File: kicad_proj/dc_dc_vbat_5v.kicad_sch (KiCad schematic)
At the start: 14 parts, among them U4 TPS563200

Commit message: checked root, dc dc and rpi sheets
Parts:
- renumbered R19 to R8, TP6 to TP8, TP7 to TP9
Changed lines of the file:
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@@
 		(dnp no)
 		(fields_autoplaced yes)
-		(property "Reference" "#PWR22"
+		(property "Reference" "#PWR21"
 			(at 172.72 99.06 0)
 			(effects
@@
 			(project "rpi_power_warden_hat"
 				(path "/8692c5de-a943-41e8-8e29-f6c5e99cda34/5bbc6f2d-46db-4213-8835-1ada71ba8330"
-					(reference "#PWR22")
-					(unit 1)
-				)
-				(path "/8692c5de-a943-41e8-8e29-f6c5e99cda34/cc58a92a-1392-4aa4-91cc-7a70ded8904f"
-					(reference "#PWR29")
+					(reference "#PWR21")
+					(unit 1)
+				)
+				(path "/8692c5de-a943-41e8-8e29-f6c5e99cda34/cc58a92a-1392-4aa4-91cc-7a70ded8904f"
+					(reference "#PWR28")
 					(unit 1)
 				)
@@
 		(dnp no)
 		(fields_autoplaced yes)
-		(property "Reference" "#PWR21"
+		(property "Reference" "#PWR20"
 			(at 128.27 101.6 0)
 			(effects
@@
 			(project "rpi_power_warden_hat"
 				(path "/8692c5de-a943-41e8-8e29-f6c5e99cda34/5bbc6f2d-46db-4213-8835-1ada71ba8330"
-					(reference "#PWR21")
-					(unit 1)
-				)
-				(path "/8692c5de-a943-41e8-8e29-f6c5e99cda34/cc58a92a-1392-4aa4-91cc-7a70ded8904f"
-					(reference "#PWR28")
+					(reference "#PWR20")
+					(unit 1)
+				)
+				(path "/8692c5de-a943-41e8-8e29-f6c5e99cda34/cc58a92a-1392-4aa4-91cc-7a70ded8904f"
+					(reference "#PWR27")
 					(unit 1)
 				)
@@
 		(dnp no)
 		(fields_autoplaced yes)
-		(property "Reference" "TP7"
-			(at 181.61 77.9779 0)
+		(property "Reference" "TP9"
+			(at 181.61 79.2479 0)
 			(effects
 				(font
@@
 				)
 				(justify left)
+				(hide yes)
 			)
 		)
@@
 			(project "rpi_power_warden_hat"
 				(path "/8692c5de-a943-41e8-8e29-f6c5e99cda34/5bbc6f2d-46db-4213-8835-1ada71ba8330"
-					(reference "TP7")
-					(unit 1)
-				)
-				(path "/8692c5de-a943-41e8-8e29-f6c5e99cda34/cc58a92a-1392-4aa4-91cc-7a70ded8904f"
 					(reference "TP9")
+					(unit 1)
+				)
+				(path "/8692c5de-a943-41e8-8e29-f6c5e99cda34/cc58a92a-1392-4aa4-91cc-7a70ded8904f"
+					(reference "TP11")
 					(unit 1)
 				)
@@
 		(dnp no)
 		(fields_autoplaced yes)
-		(property "Reference" "#PWR23"
+		(property "Reference" "#PWR22"
 			(at 185.42 99.06 0)
 			(effects
@@
 			(project "rpi_power_warden_hat"
 				(path "/8692c5de-a943-41e8-8e29-f6c5e99cda34/5bbc6f2d-46db-4213-8835-1ada71ba8330"
-					(reference "#PWR23")
-					(unit 1)
-				)
-				(path "/8692c5de-a943-41e8-8e29-f6c5e99cda34/cc58a92a-1392-4aa4-91cc-7a70ded8904f"
-					(reference "#PWR30")
+					(reference "#PWR22")
+					(unit 1)
+				)
+				(path "/8692c5de-a943-41e8-8e29-f6c5e99cda34/cc58a92a-1392-4aa4-91cc-7a70ded8904f"
+					(reference "#PWR29")
 					(unit 1)
 				)
@@
 		(dnp no)
 		(fields_autoplaced yes)
-		(property "Reference" "#PWR20"
+		(property "Reference" "#PWR19"
 			(at 97.79 104.14 0)
 			(effects
@@
 			(project "rpi_power_warden_hat"
 				(path "/8692c5de-a943-41e8-8e29-f6c5e99cda34/5bbc6f2d-46db-4213-8835-1ada71ba8330"
-					(reference "#PWR20")
-					(unit 1)
-				)
-				(path "/8692c5de-a943-41e8-8e29-f6c5e99cda34/cc58a92a-1392-4aa4-91cc-7a70ded8904f"
-					(reference "#PWR27")
+					(reference "#PWR19")
+					(unit 1)
+				)
+				(path "/8692c5de-a943-41e8-8e29-f6c5e99cda34/cc58a92a-1392-4aa4-91cc-7a70ded8904f"
+					(reference "#PWR26")
 					(unit 1)
 				)
@@
 		(dnp no)
 		(fields_autoplaced yes)
-		(property "Reference" "#PWR25"
+		(property "Reference" "#PWR24"
 			(at 217.17 120.65 0)
 			(effects
@@
 			(project "rpi_power_warden_hat"
 				(path "/8692c5de-a943-41e8-8e29-f6c5e99cda34/5bbc6f2d-46db-4213-8835-1ada71ba8330"
-					(reference "#PWR25")
-					(unit 1)
-				)
-				(path "/8692c5de-a943-41e8-8e29-f6c5e99cda34/cc58a92a-1392-4aa4-91cc-7a70ded8904f"
-					(reference "#PWR32")
+					(reference "#PWR24")
+					(unit 1)
+				)
+				(path "/8692c5de-a943-41e8-8e29-f6c5e99cda34/cc58a92a-1392-4aa4-91cc-7a70ded8904f"
+					(reference "#PWR31")
 					(unit 1)
 				)
@@
 		(dnp no)
 		(fields_autoplaced yes)
-		(property "Reference" "TP6"
-			(at 110.49 77.9779 0)
+		(property "Reference" "TP8"
+			(at 110.49 79.2479 0)
 			(effects
 				(font
@@
 				)
 				(justify left)
+				(hide yes)
 			)
 		)
@@
 			(project "rpi_power_warden_hat"
 				(path "/8692c5de-a943-41e8-8e29-f6c5e99cda34/5bbc6f2d-46db-4213-8835-1ada71ba8330"
-					(reference "TP6")
-					(unit 1)
-				)
-				(path "/8692c5de-a943-41e8-8e29-f6c5e99cda34/cc58a92a-1392-4aa4-91cc-7a70ded8904f"
 					(reference "TP8")
+					(unit 1)
+				)
+				(path "/8692c5de-a943-41e8-8e29-f6c5e99cda34/cc58a92a-1392-4aa4-91cc-7a70ded8904f"
+					(reference "TP10")
 					(unit 1)
 				)
@@
 		(dnp no)
 		(fields_autoplaced yes)
-		(property "Reference" "#PWR19"
+		(property "Reference" "#PWR18"
 			(at 85.09 104.14 0)
 			(effects
@@
 			(project "rpi_power_warden_hat"
 				(path "/8692c5de-a943-41e8-8e29-f6c5e99cda34/5bbc6f2d-46db-4213-8835-1ada71ba8330"
-					(reference "#PWR19")
-					(unit 1)
-				)
-				(path "/8692c5de-a943-41e8-8e29-f6c5e99cda34/cc58a92a-1392-4aa4-91cc-7a70ded8904f"
-					(reference "#PWR26")
+					(reference "#PWR18")
+					(unit 1)
+				)
+				(path "/8692c5de-a943-41e8-8e29-f6c5e99cda34/cc58a92a-1392-4aa4-91cc-7a70ded8904f"
+					(reference "#PWR25")
 					(unit 1)
 				)
@@
 		(on_board yes)
 		(dnp no)
-		(property "Reference" "R19"
+		(property "Reference" "R8"
 			(at 114.3 87.884 90)
 			(effects
@@
 			(project "rpi_power_warden_hat"
 				(path "/8692c5de-a943-41e8-8e29-f6c5e99cda34/5bbc6f2d-46db-4213-8835-1ada71ba8330"
-					(reference "R19")
+					(reference "R8")
 					(unit 1)
 				)
@@
 		(dnp no)
 		(fields_autoplaced yes)
-		(property "Reference" "#PWR24"
+		(property "Reference" "#PWR23"
 			(at 196.85 119.38 0)
 			(effects
@@
 			(project "rpi_power_warden_hat"
 				(path "/8692c5de-a943-41e8-8e29-f6c5e99cda34/5bbc6f2d-46db-4213-8835-1ada71ba8330"
-					(reference "#PWR24")
-					(unit 1)
-				)
-				(path "/8692c5de-a943-41e8-8e29-f6c5e99cda34/cc58a92a-1392-4aa4-91cc-7a70ded8904f"
-					(reference "#PWR31")
-					(unit 1)
-				)
+					(reference "#PWR23")
+					(unit 1)
+				)
+				(path "/8692c5de-a943-41e8-8e29-f6c5e99cda34/cc58a92a-1392-4aa4-91cc-7a70ded8904f"
+					(reference "#PWR30")
+					(unit 1)
+				)

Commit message: checked all the schematics
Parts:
- TP8, TP9: now left out of the parts list
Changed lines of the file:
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@@
 		(unit 1)
 		(exclude_from_sim no)
-		(in_bom yes)
-		(on_board yes)
-		(dnp no)
-		(fields_autoplaced yes)
+		(in_bom no)
+		(on_board yes)
+		(dnp no)
 		(property "Reference" "TP9"
-			(at 181.61 79.2479 0)
+			(at 177.292 76.962 0)
 			(effects
 				(font
@@
 		(unit 1)
 		(exclude_from_sim no)
-		(in_bom yes)
-		(on_board yes)
-		(dnp no)
-		(fields_autoplaced yes)
+		(in_bom no)
+		(on_board yes)
+		(dnp no)
 		(property "Reference" "TP8"
-			(at 110.49 79.2479 0)
-			(effects
-				(font
+			(at 106.172 76.962 0)
+			(effects
+				(font

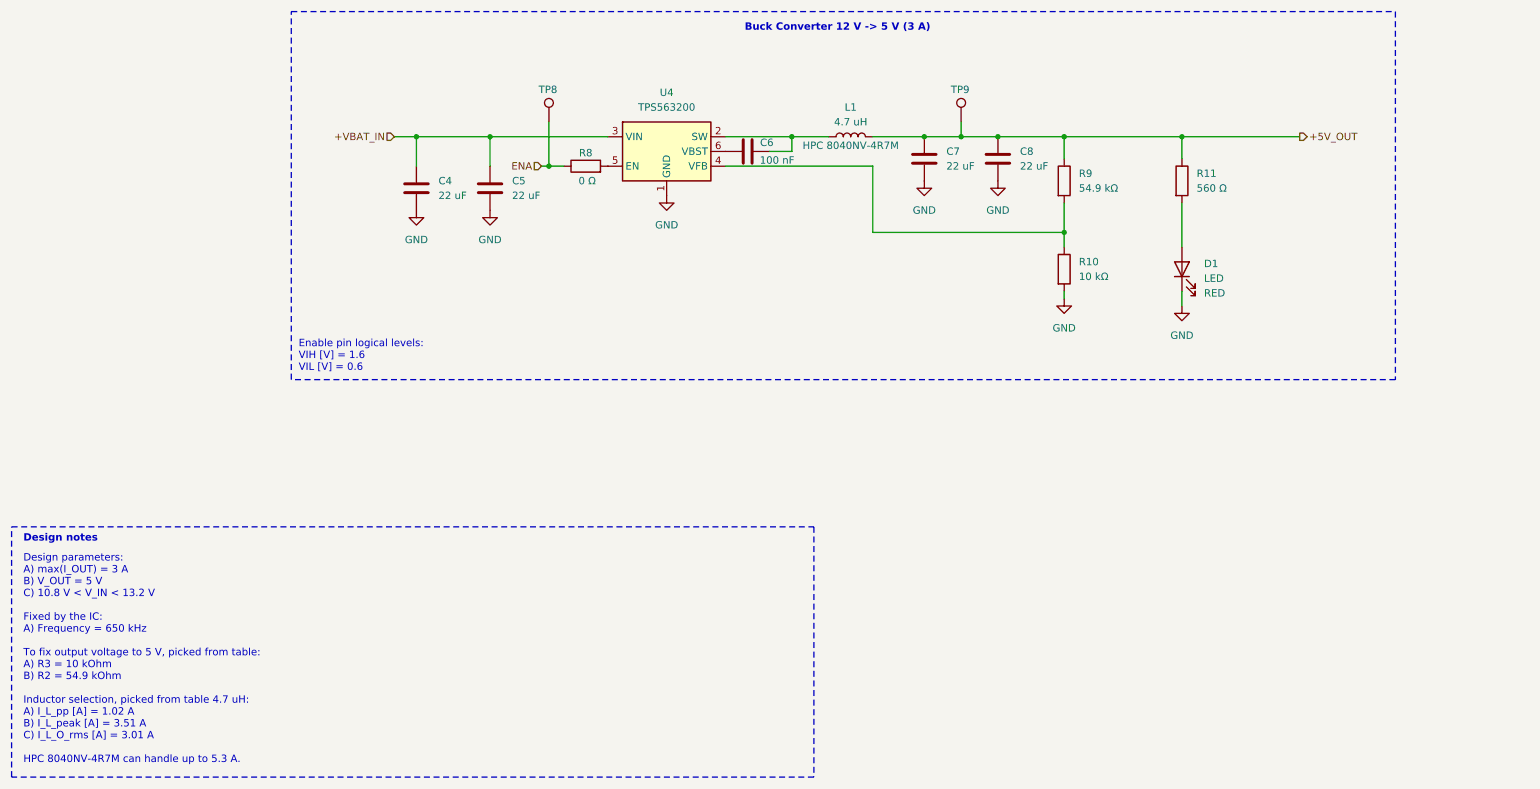
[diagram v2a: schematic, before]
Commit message: add ideal diode to 5v power supply
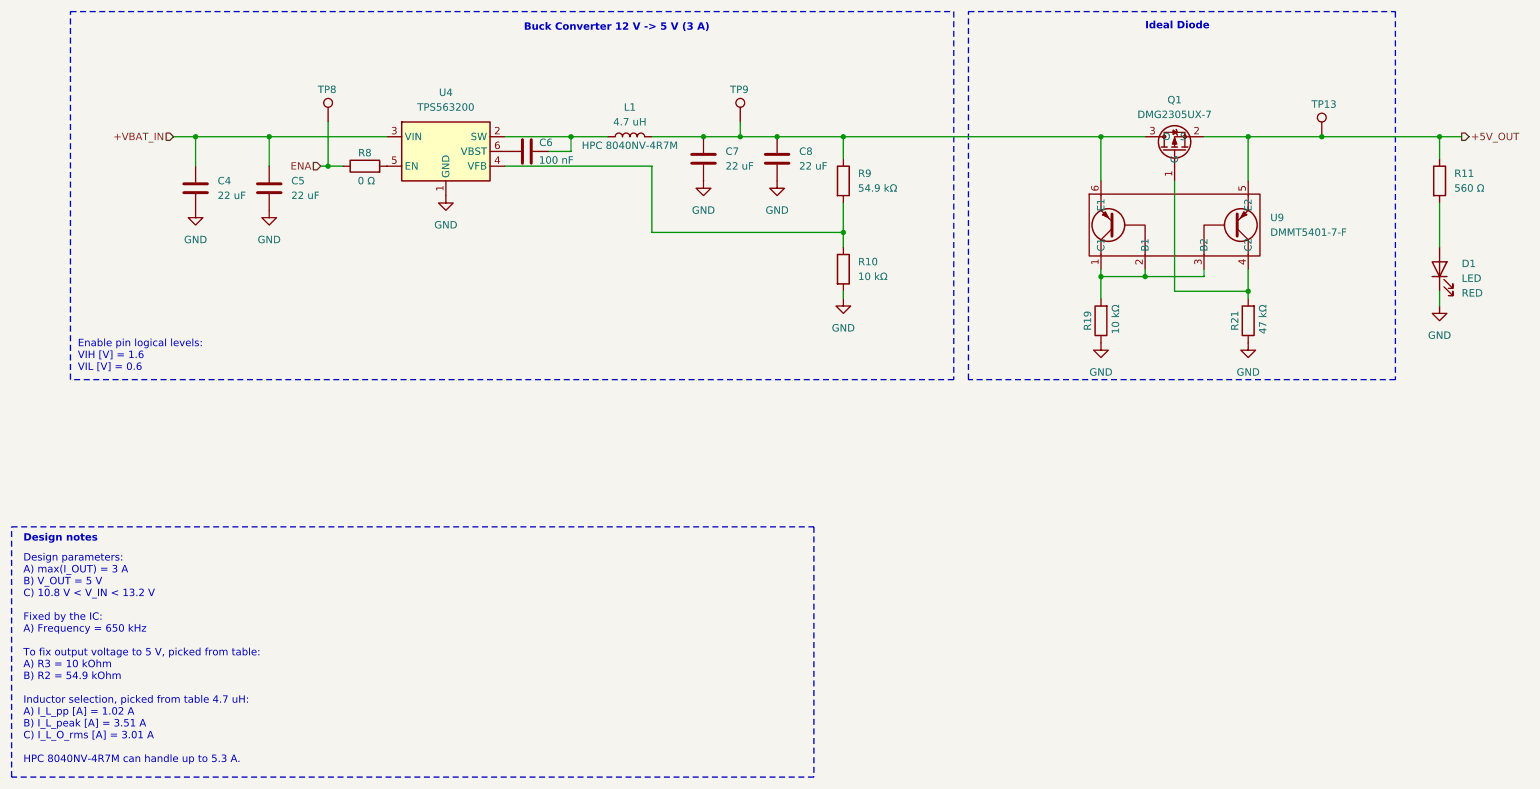
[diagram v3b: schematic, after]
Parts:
- added Q1: DMG2305UX-7, rpi_power_warden_hat:SOT-23, symbol rpi_power_warden_hat:DMG2305UX-7
- added R19: 10 kΩ, Resistor_SMD:R_0603_1608Metric_Pad0.98x0.95mm_HandSolder, symbol Device:R
- added R21: 47 kΩ, Resistor_SMD:R_0603_1608Metric_Pad0.98x0.95mm_HandSolder, symbol Device:R
- added TP13: TestPoint, TestPoint:TestPoint_Pad_D2.5mm, symbol Connector:TestPoint
- added U9: DMMT5401-7-F, rpi_power_warden_hat:SOT-23-6, symbol rpi_power_warden_hat:DMMT5401-7-F
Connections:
- net +5V_OUT: now also Q1.2 (S), TP13.1, U9.5 (E2); no longer C7.1, C8.1, L1.2, R9.1, TP9.1
- net GND: now also R19.1, R21.1
- new net: R19.2, U9.1 (C1), U9.2 (B1), U9.3 (B2)
- new net: Q1.1 (G), R21.2, U9.4 (C2)
- new net: C7.1, C8.1, L1.2, Q1.3 (D), R9.1, TP9.1, U9.6 (E1)
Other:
- note added: "Ideal Diode"
- moved on the sheet: C4, C5, C6, C7, C8, D1, L1, R10, R11, R8, R9, TP8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

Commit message: re-annotate schematic
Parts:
- renumbered R19 to R11, R21 to R12, R11 to R13, TP13 to TP10, U9 to U7
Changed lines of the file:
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@@
 		(dnp no)
 		(fields_autoplaced yes)
-		(property "Reference" "U9"
+		(property "Reference" "U7"
 			(at 232.41 99.0599 0)
 			(effects
@@
 			(project ""
 				(path "/8692c5de-a943-41e8-8e29-f6c5e99cda34/5bbc6f2d-46db-4213-8835-1ada71ba8330"
-					(reference "U2")
-					(unit 1)
-				)
-				(path "/8692c5de-a943-41e8-8e29-f6c5e99cda34/cc58a92a-1392-4aa4-91cc-7a70ded8904f"
-					(reference "U9")
+					(reference "U5")
+					(unit 1)
+				)
+				(path "/8692c5de-a943-41e8-8e29-f6c5e99cda34/cc58a92a-1392-4aa4-91cc-7a70ded8904f"
+					(reference "U7")
 					(unit 1)
 				)
@@
 				)
 				(path "/8692c5de-a943-41e8-8e29-f6c5e99cda34/cc58a92a-1392-4aa4-91cc-7a70ded8904f"
-					(reference "#PWR28")
+					(reference "#PWR30")
 					(unit 1)
 				)
@@
 		(dnp no)
 		(fields_autoplaced yes)
-		(property "Reference" "#PWR42"
+		(property "Reference" "#PWR25"
 			(at 228.6 127 0)
 			(effects
@@
 			(project "rpi_power_warden_hat"
 				(path "/8692c5de-a943-41e8-8e29-f6c5e99cda34/5bbc6f2d-46db-4213-8835-1ada71ba8330"
-					(reference "#PWR42")
-					(unit 1)
-				)
-				(path "/8692c5de-a943-41e8-8e29-f6c5e99cda34/cc58a92a-1392-4aa4-91cc-7a70ded8904f"
-					(reference "#PWR43")
+					(reference "#PWR25")
+					(unit 1)
+				)
+				(path "/8692c5de-a943-41e8-8e29-f6c5e99cda34/cc58a92a-1392-4aa4-91cc-7a70ded8904f"
+					(reference "#PWR34")
 					(unit 1)
 				)
@@
 				)
 				(path "/8692c5de-a943-41e8-8e29-f6c5e99cda34/cc58a92a-1392-4aa4-91cc-7a70ded8904f"
-					(reference "R14")
+					(reference "R16")
 					(unit 1)
 				)
@@
 				)
 				(path "/8692c5de-a943-41e8-8e29-f6c5e99cda34/cc58a92a-1392-4aa4-91cc-7a70ded8904f"
-					(reference "#PWR27")
+					(reference "#PWR29")
 					(unit 1)
 				)
@@
 				)
 				(path "/8692c5de-a943-41e8-8e29-f6c5e99cda34/cc58a92a-1392-4aa4-91cc-7a70ded8904f"
-					(reference "TP11")
+					(reference "TP12")
 					(unit 1)
 				)
@@
 				)
 				(path "/8692c5de-a943-41e8-8e29-f6c5e99cda34/cc58a92a-1392-4aa4-91cc-7a70ded8904f"
-					(reference "#PWR29")
+					(reference "#PWR31")
 					(unit 1)
 				)
@@
 		(on_board yes)
 		(dnp no)
-		(property "Reference" "R19"
+		(property "Reference" "R11"
 			(at 200.914 116.84 90)
 			(effects
@@
 			(project "rpi_power_warden_hat"
 				(path "/8692c5de-a943-41e8-8e29-f6c5e99cda34/5bbc6f2d-46db-4213-8835-1ada71ba8330"
-					(reference "R19")
-					(unit 1)
-				)
-				(path "/8692c5de-a943-41e8-8e29-f6c5e99cda34/cc58a92a-1392-4aa4-91cc-7a70ded8904f"
-					(reference "R20")
+					(reference "R11")
+					(unit 1)
+				)
+				(path "/8692c5de-a943-41e8-8e29-f6c5e99cda34/cc58a92a-1392-4aa4-91cc-7a70ded8904f"
+					(reference "R17")
 					(unit 1)
 				)
@@
 		(on_board yes)
 		(dnp no)
-		(property "Reference" "R11"
+		(property "Reference" "R13"
 			(at 264.16 91.4399 0)
 			(effects
@@
 			(project "rpi_power_warden_hat"
 				(path "/8692c5de-a943-41e8-8e29-f6c5e99cda34/5bbc6f2d-46db-4213-8835-1ada71ba8330"
-					(reference "R11")
-					(unit 1)
-				)
-				(path "/8692c5de-a943-41e8-8e29-f6c5e99cda34/cc58a92a-1392-4aa4-91cc-7a70ded8904f"
-					(reference "R15")
+					(reference "R13")
+					(unit 1)
+				)
+				(path "/8692c5de-a943-41e8-8e29-f6c5e99cda34/cc58a92a-1392-4aa4-91cc-7a70ded8904f"
+					(reference "R19")
 					(unit 1)
 				)
@@
 		(dnp no)
 		(fields_autoplaced yes)
-		(property "Reference" "#PWR40"
+		(property "Reference" "#PWR24"
 			(at 203.2 127 0)
 			(effects
@@
 			(project "rpi_power_warden_hat"
 				(path "/8692c5de-a943-41e8-8e29-f6c5e99cda34/5bbc6f2d-46db-4213-8835-1ada71ba8330"
-					(reference "#PWR40")
-					(unit 1)
-				)
-				(path "/8692c5de-a943-41e8-8e29-f6c5e99cda34/cc58a92a-1392-4aa4-91cc-7a70ded8904f"
-					(reference "#PWR41")
+					(reference "#PWR24")
+					(unit 1)
+				)
+				(path "/8692c5de-a943-41e8-8e29-f6c5e99cda34/cc58a92a-1392-4aa4-91cc-7a70ded8904f"
+					(reference "#PWR33")
 					(unit 1)
 				)
@@
 				)
 				(path "/8692c5de-a943-41e8-8e29-f6c5e99cda34/cc58a92a-1392-4aa4-91cc-7a70ded8904f"
-					(reference "#PWR26")
+					(reference "#PWR28")
 					(unit 1)
 				)
@@
 		(dnp no)
 		(fields_autoplaced yes)
-		(property "Reference" "#PWR24"
+		(property "Reference" "#PWR26"
 			(at 261.62 120.65 0)
 			(effects
@@
 			(project "rpi_power_warden_hat"
 				(path "/8692c5de-a943-41e8-8e29-f6c5e99cda34/5bbc6f2d-46db-4213-8835-1ada71ba8330"
-					(reference "#PWR24")
-					(unit 1)
-				)
-				(path "/8692c5de-a943-41e8-8e29-f6c5e99cda34/cc58a92a-1392-4aa4-91cc-7a70ded8904f"
-					(reference "#PWR31")
+					(reference "#PWR26")
+					(unit 1)
+				)
+				(path "/8692c5de-a943-41e8-8e29-f6c5e99cda34/cc58a92a-1392-4aa4-91cc-7a70ded8904f"
+					(reference "#PWR35")
 					(unit 1)
 				)
@@
 		(on_board yes)
 		(dnp no)
-		(property "Reference" "TP13"
+		(property "Reference" "TP10"
 			(at 239.522 79.502 0)
 			(effects
@@
 			(project "rpi_power_warden_hat"
 				(path "/8692c5de-a943-41e8-8e29-f6c5e99cda34/5bbc6f2d-46db-4213-8835-1ada71ba8330"
+					(reference "TP10")
+					(unit 1)
+				)
+				(path "/8692c5de-a943-41e8-8e29-f6c5e99cda34/cc58a92a-1392-4aa4-91cc-7a70ded8904f"
 					(reference "TP13")
-					(unit 1)
-				)
-				(path "/8692c5de-a943-41e8-8e29-f6c5e99cda34/cc58a92a-1392-4aa4-91cc-7a70ded8904f"
-					(reference "TP14")
 					(unit 1)
 				)
@@
 				)
 				(path "/8692c5de-a943-41e8-8e29-f6c5e99cda34/cc58a92a-1392-4aa4-91cc-7a70ded8904f"
-					(reference "TP10")
+					(reference "TP11")
 					(unit 1)
 				)
@@
 				)
 				(path "/8692c5de-a943-41e8-8e29-f6c5e99cda34/cc58a92a-1392-4aa4-91cc-7a70ded8904f"
-					(reference "#PWR25")
+					(reference "#PWR27")
 					(unit 1)
 				)
@@
 				)
 				(path "/8692c5de-a943-41e8-8e29-f6c5e99cda34/cc58a92a-1392-4aa4-91cc-7a70ded8904f"
-					(reference "R12")
+					(reference "R14")
 					(unit 1)
 				)
@@
 				)
 				(path "/8692c5de-a943-41e8-8e29-f6c5e99cda34/cc58a92a-1392-4aa4-91cc-7a70ded8904f"
-					(reference "#PWR30")
+					(reference "#PWR32")
 					(unit 1)
 				)
@@
 				)
 				(path "/8692c5de-a943-41e8-8e29-f6c5e99cda34/cc58a92a-1392-4aa4-91cc-7a70ded8904f"
-					(reference "U5")
+					(reference "U6")
 					(unit 1)
 				)
@@
 				)
 				(path "/8692c5de-a943-41e8-8e29-f6c5e99cda34/cc58a92a-1392-4aa4-91cc-7a70ded8904f"
-					(reference "R13")
+					(reference "R15")
 					(unit 1)
 				)
@@
 		(on_board yes)
 		(dnp no)
-		(property "Reference" "R21"
+		(property "Reference" "R12"
 			(at 226.314 116.84 90)
 			(effects
@@
 			(project "rpi_power_warden_hat"
 				(path "/8692c5de-a943-41e8-8e29-f6c5e99cda34/5bbc6f2d-46db-4213-8835-1ada71ba8330"
-					(reference "R21")
-					(unit 1)
-				)
-				(path "/8692c5de-a943-41e8-8e29-f6c5e99cda34/cc58a92a-1392-4aa4-91cc-7a70ded8904f"
-					(reference "R22")
-					(unit 1)
-				)
+					(reference "R12")
+					(unit 1)
+				)
+				(path "/8692c5de-a943-41e8-8e29-f6c5e99cda34/cc58a92a-1392-4aa4-91cc-7a70ded8904f"
+					(reference "R18")
+					(unit 1)
+				)

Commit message: remove whitespaces from some resistors's mpn, add mpn to pnp in zvd symbol and regenerate bom
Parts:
- R13: mpn ERJ-3EKF5600V -> ERJ-3EKF5600V
- U7: manufacturer (none) -> Diodes Incorporated; mpn (none) -> DMMT5401-7-F
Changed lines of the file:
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@@
+			)
+		)
+		(property "mpn" "DMMT5401-7-F"
+			(at 215.9 100.33 0)
+			(effects
+				(font
+					(size 1.27 1.27)
+				)
+				(hide yes)
+			)
+		)
+		(property "manufacturer" "Diodes Incorporated"
+			(at 215.9 100.33 0)
+			(effects
+				(font
+					(size 1.27 1.27)
+				)
+				(hide yes)
 			)
 		)
@@
 			)
 		)
-		(property "mpn" " ERJ-3EKF5600V"
+		(property "mpn" "ERJ-3EKF5600V"
 			(at 261.62 92.71 0)
 			(effects
